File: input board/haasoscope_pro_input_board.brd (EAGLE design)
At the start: 85 x 74 mm, 51 parts, among them IC1 LMH5401IRMST, IC2 LMH6401IRMZR, IC3 SN74AVC4T774PWR, IC4 OPA693ID, IC6 DAC8562SDGSR, IC7 TLV9102IPWR, J1 8pin, J3 2X4P-2.54, J4 8pin

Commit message: power connector etc
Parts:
- removed J3: 2X4P-2.54, Seeed-Connector:H2X4-2.54
- moved J4 92.3 mm to (83.0, 20.0)
- moved C9 76.4 mm to (77.0, 4.00)
- moved IC3 74.4 mm to (71.0, 5.00)
- moved C10 72.2 mm to (74.0, 9.00), turned to 180 degrees
- moved D1 62.0 mm to (17.0, 8.00)
- moved R12 62.0 mm to (13.0, 8.00)
- moved J1 59.1 mm to (52.0, 10.0), turned to 0 degrees
- moved C13 58.2 mm to (39.0, 2.00), turned to 180 degrees
- moved R18 57.7 mm to (36.0, 3.00), turned to 0 degrees
- moved D2 55.0 mm to (17.0, 12.0)
- moved R13 55.0 mm to (13.0, 12.0)
- moved R17 54.1 mm to (36.0, 5.00), turned to 0 degrees
- moved C15 53.2 mm to (51.0, 3.00), turned to 180 degrees
- moved IC6 53.2 mm to (56.0, 4.00), turned to 0 degrees
- moved IC7 50.7 mm to (42.0, 5.00), turned to 180 degrees
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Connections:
- net 2V5OUT renamed 2V5DACOUT
- net 3V3: no longer J4.7
- net AMPSCLK: no longer J3.8
- net AMPSCS: no longer J3.7
- net AMPSDI: no longer J3.6
- net AMPSDO: no longer J3.5
- net GND: no longer J3.1, J3.4, J4.8
- net VS+: now also J4.7; no longer J3.2
- net VS-: now also J4.8; no longer J3.3
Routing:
- net 3V3: track 140.7 -> 7.27 mm
- net AMPSDO: track 122.8 -> 3.40 mm
- net AMPSDI: track 92.8 -> 1.90 mm
- net AMPSCS: track 91.6 -> 4.90 mm
- net DACAMPOUT1: track 110.3 -> 23.8 mm, vias 2 -> 0
- net AMPSCLK: track 91.4 -> 6.40 mm
- net GND: track 60.2 -> 36.5 mm, vias 30 -> 18
- net DACOUT2: track 16.7 -> 0.00 mm
- net VS+: track 56.3 -> 40.0 mm, vias 16 -> 8
- net VS-: track 38.1 -> 22.7 mm, vias 22 -> 8
- net DACOUT1: track 18.1 -> 2.66 mm
- net SCLK3: track 11.5 -> 0.00 mm
- net AMPOUTSMA_N: track 11.3 -> 0.00 mm
- net 2V5DACOUT: track 47.0 -> 36.1 mm
- net SCS3: track 10.7 -> 0.00 mm
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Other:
- board size 85 x 74 mm -> 75 x 42 mm
- board text added: "Haasoscope Pro Input board, v1.1 by Dr. Andy Haas August 2024"
- board text removed: "2V5OUT"
- board text removed: "AmpSCLK"
- board text removed: "AmpSCS"
- board text removed: "AmpSDI"
- board text removed: "AmpSDO"
- board text removed: "DACDIN"
- board text removed: "DACOUT1"
- board text removed: "DACOUT2"
- board text removed: "DACSCLK"
- board text removed: "DACSYNC"
- board text removed: "Haasoscope Pro Input board, v1.0 by Dr. Andy Haas July 2024"

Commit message: power connector etc
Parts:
- added R21, R22: 0, MF_Passives:R0402
- AMPOUT+, AMPOUT-: value BU-SMB-V -> (none); device con-coax:BU-SMB-V -> adafruit:SMA_EDGELAUNCH
- moved D2 51.6 mm to (68.5, 8.50)
- moved R13 51.6 mm to (64.5, 8.50)
- moved AOUT+ 15.5 mm to (44.0, 42.5)
- moved R15 14.5 mm to (25.6, 28.1)
- moved AIN 14.5 mm to (15.0, 34.5)
- moved C1 14.5 mm to (31.0, 39.5)
- moved C2 14.5 mm to (29.0, 39.5)
- moved C3 14.5 mm to (31.0, 31.5)
- moved C4 14.5 mm to (29.0, 31.5)
- moved C5 14.5 mm to (67.0, 31.5)
- moved C6 14.5 mm to (65.3, 31.5)
- moved C7 14.5 mm to (67.0, 39.5)
- moved C8 14.5 mm to (65.0, 39.5)
- moved IC1 14.5 mm to (30.0, 35.5)
- moved IC2 14.5 mm to (66.0, 35.5)
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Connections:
- new net N$4: AOUT-.1, R22.P$2
- new net N$6: AOUT+.1, R21.P$2
- net AMPOUTSMA_N: now also AMPOUT-.P; no longer AMPOUT-.1
- net AMPOUTSMA_P: now also AMPOUT+.P; no longer AMPOUT+.1
- net AOUTSMA_N: now also R22.P$1; no longer AOUT-.1
- net AOUTSMA_P: now also R21.P$1; no longer AOUT+.1
- net GND: now also AMPOUT+.GND@1, AMPOUT+.GND@2, AMPOUT+.GND@3, AMPOUT+.GND@4, AMPOUT-.GND@1, AMPOUT-.GND@2, AMPOUT-.GND@3, AMPOUT-.GND@4; no longer AMPOUT+.2, AMPOUT+.3, AMPOUT+.4, AMPOUT+.5, AMPOUT-.2, AMPOUT-.3, AMPOUT-.4, AMPOUT-.5
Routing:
- net 2V5DACOUT: track 36.1 -> 0.00 mm
- net DACAMPOUT1: track 23.8 -> 0.00 mm
- net N$3: track 18.8 -> 0.00 mm
- net VS+: track 40.0 -> 22.5 mm
- net 1V25OUT-: track 10.5 -> 0.00 mm
- net OFFSETOUT: track 10.2 -> 0.00 mm
- net 3V3: track 7.27 -> 0.00 mm
- net N$5: track 5.10 -> 0.00 mm
- net N$6: track 0.00 -> 4.45 mm
- net N$4: track 0.00 -> 4.45 mm
- net VS-: track 22.7 -> 18.5 mm
- net AOUTSMA_N: track 23.9 -> 20.6 mm
- net AOUTSMA_P: track 24.4 -> 21.3 mm
- net DACOUT1: track 2.66 -> 0.00 mm
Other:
- board size 75 x 42 mm -> 75 x 50 mm
- board text added: "2V5DACOUT"
- board text added: "DACDIN"
- board text added: "DACOUT1"
- board text added: "DACOUT2"
- board text added: "DACSCLK"
- board text added: "DACSYNC"

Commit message: v1.1 routed
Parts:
- moved C12 3.91 mm to (28.6, 20.8), turned to 180 degrees
- moved C9 2.50 mm to (72.5, 18.5)
- turned R19 to 0 degrees
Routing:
- net 3V3: track 0.00 -> 65.4 mm, vias 0 -> 2
- net VS+: track 22.5 -> 70.9 mm
- net 2V5DACOUT: track 0.00 -> 44.2 mm, vias 0 -> 2
- net AMPSCLK: track 6.40 -> 47.7 mm, vias 0 -> 2
- net GND: track 36.9 -> 72.9 mm, vias 18 -> 64
- net N$3: track 0.00 -> 25.3 mm
- net DACSCLK: track 0.00 -> 24.9 mm
- net AMPSDI: track 1.90 -> 25.6 mm, vias 0 -> 2
- net DACOUT2: track 0.00 -> 23.4 mm, vias 0 -> 2
- net SDO3: track 0.00 -> 23.2 mm
- net SCLK3: track 0.00 -> 22.8 mm
- net SDI3: track 0.00 -> 22.8 mm
- net DACSYNC: track 0.00 -> 22.4 mm, vias 0 -> 2
- net SCS3: track 0.00 -> 22.2 mm
- net DACOUT1: track 0.00 -> 21.9 mm
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
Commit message: minor-fix ampout for jlcpcb
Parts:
- AMPOUT+: value (none) -> out+
- AMPOUT-: value (none) -> out-
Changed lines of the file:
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@@
 <drawing>
 <settings>
-<setting alwaysvectorfont="yes"/>
+<setting alwaysvectorfont="no"/>
 <setting verticaltext="up"/>
 </settings>
@@
 <attribute name="PROD_ID" value="CONN-08438" x="40.5" y="2.5" size="0.8128" layer="27" display="off"/>
 </element>
-<element name="AMPOUT-" library="adafruit" package="SMA_EDGELAUNCH" value="" x="84.5" y="29" smashed="yes" rot="R180">
+<element name="AMPOUT-" library="adafruit" package="SMA_EDGELAUNCH" value="out-" x="84.5" y="29" smashed="yes" rot="R180">
 <attribute name="NAME" x="79.485" y="25.92" size="1.016" layer="25" rot="R90"/>
 <attribute name="VALUE" x="79.42" y="36.62" size="0.8128" layer="27" ratio="10"/>
 </element>
-<element name="AMPOUT+" library="adafruit" package="SMA_EDGELAUNCH" value="" x="84.5" y="42" smashed="yes" rot="R180">
+<element name="AMPOUT+" library="adafruit" package="SMA_EDGELAUNCH" value="out+" x="84.5" y="42" smashed="yes" rot="R180">
 <attribute name="NAME" x="79.485" y="38.92" size="1.016" layer="25" rot="R90"/>
 <attribute name="VALUE" x="79.42" y="49.62" size="0.8128" layer="27" ratio="10"/>

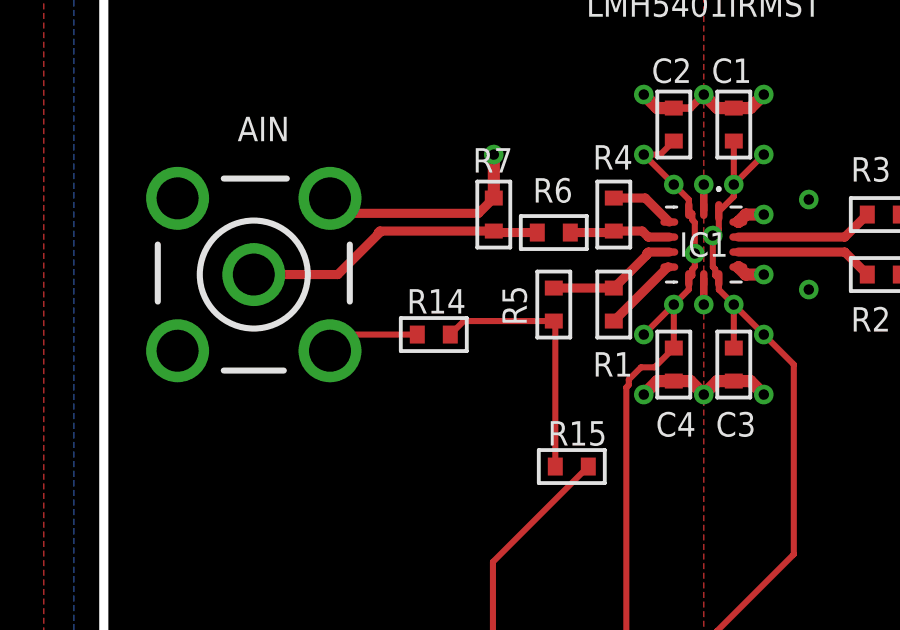
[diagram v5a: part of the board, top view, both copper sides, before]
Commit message: working dac offset
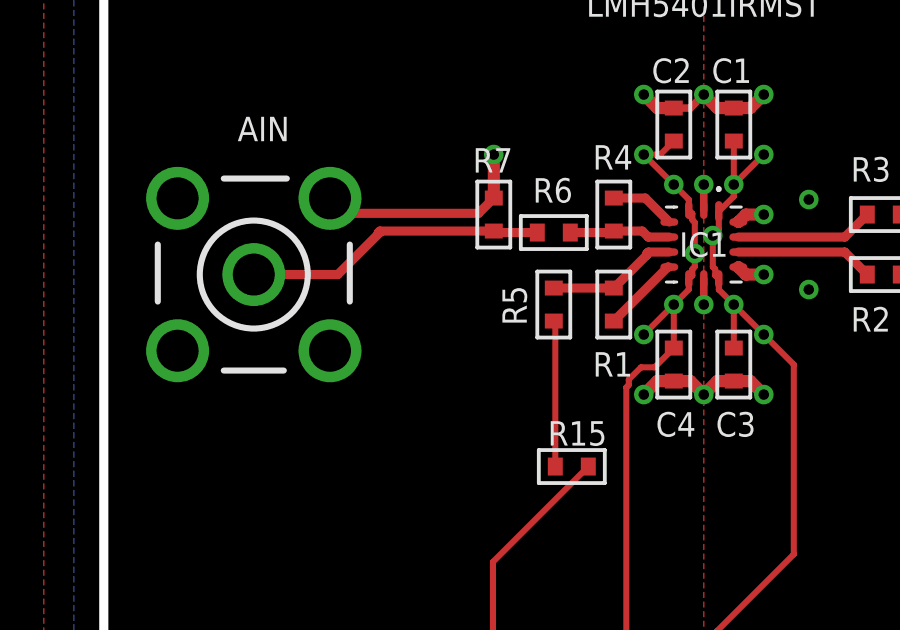
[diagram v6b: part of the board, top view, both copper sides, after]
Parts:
- removed R14: 0, MF_Passives:R0402
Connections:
- net AOFFSET: no longer R14.P$2
- net GND: no longer R14.P$1
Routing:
- net AOFFSET: track 8.51 -> 4.87 mm
- net GND: track 72.9 -> 70.5 mm
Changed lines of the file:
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@@
 <attribute name="WATTAGE" value="" x="64.5" y="8.5" size="0.8128" layer="27" display="off"/>
-</element>
-<element name="R14" library="MF_Passives" package="R0402" value="0" x="21" y="32.5" smashed="yes">
-<attribute name="HOUSEPART" value="" x="21" y="32.5" size="0.8128" layer="27" display="off"/>
-<attribute name="MPN" value="" x="21" y="32.5" size="0.8128" layer="27" display="off"/>
-<attribute name="NAME" x="20.1" y="33.2" size="0.8128" layer="25" font="vector"/>
-<attribute name="POPULATE" value="1" x="21" y="32.5" size="0.8128" layer="27" display="off"/>
-<attribute name="TOLERANCE" value="" x="21" y="32.5" size="0.8128" layer="27" display="off"/>
-<attribute name="URL" value="" x="21" y="32.5" size="0.8128" layer="27" display="off"/>
-<attribute name="VOLTAGE" value="" x="21" y="32.5" size="0.8128" layer="27" display="off"/>
-<attribute name="WATTAGE" value="" x="21" y="32.5" size="0.8128" layer="27" display="off"/>
 </element>
 <element name="R15" library="MF_Passives" package="R0402" value="0" x="25.6" y="28.1" smashed="yes" rot="R180">
@@
 <contactref element="R12" pad="P$1"/>
 <contactref element="R13" pad="P$1"/>
-<contactref element="R14" pad="P$1"/>
 <contactref element="C11" pad="P$2"/>
 <contactref element="C12" pad="P$2"/>
@@
 <contactref element="J1" pad="3"/>
 <wire x1="17.54" y1="31.96" x2="18.08" y2="32.5" width="0.2032" layer="1"/>
-<wire x1="18.08" y1="32.5" x2="20.45" y2="32.5" width="0.2032" layer="1"/>
 <contactref element="AMPOUT-" pad="GND@1"/>
 <contactref element="AMPOUT+" pad="GND@1"/>
@@
 <signal name="AOFFSET">
 <contactref element="R5" pad="P$1"/>
-<contactref element="R14" pad="P$2"/>
 <contactref element="R15" pad="P$2"/>
-<wire x1="21.55" y1="32.5" x2="22" y2="32.95" width="0.2032" layer="1"/>
-<wire x1="22" y1="32.95" x2="25" y2="32.95" width="0.2032" layer="1"/>
 <wire x1="25" y1="32.95" x2="25.05" y2="32.9" width="0.2032" layer="1"/>
 <wire x1="25.05" y1="32.9" x2="25.05" y2="28.1" width="0.2032" layer="1"/>
